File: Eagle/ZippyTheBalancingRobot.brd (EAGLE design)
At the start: 81.3 x 81.3 mm, 33 parts

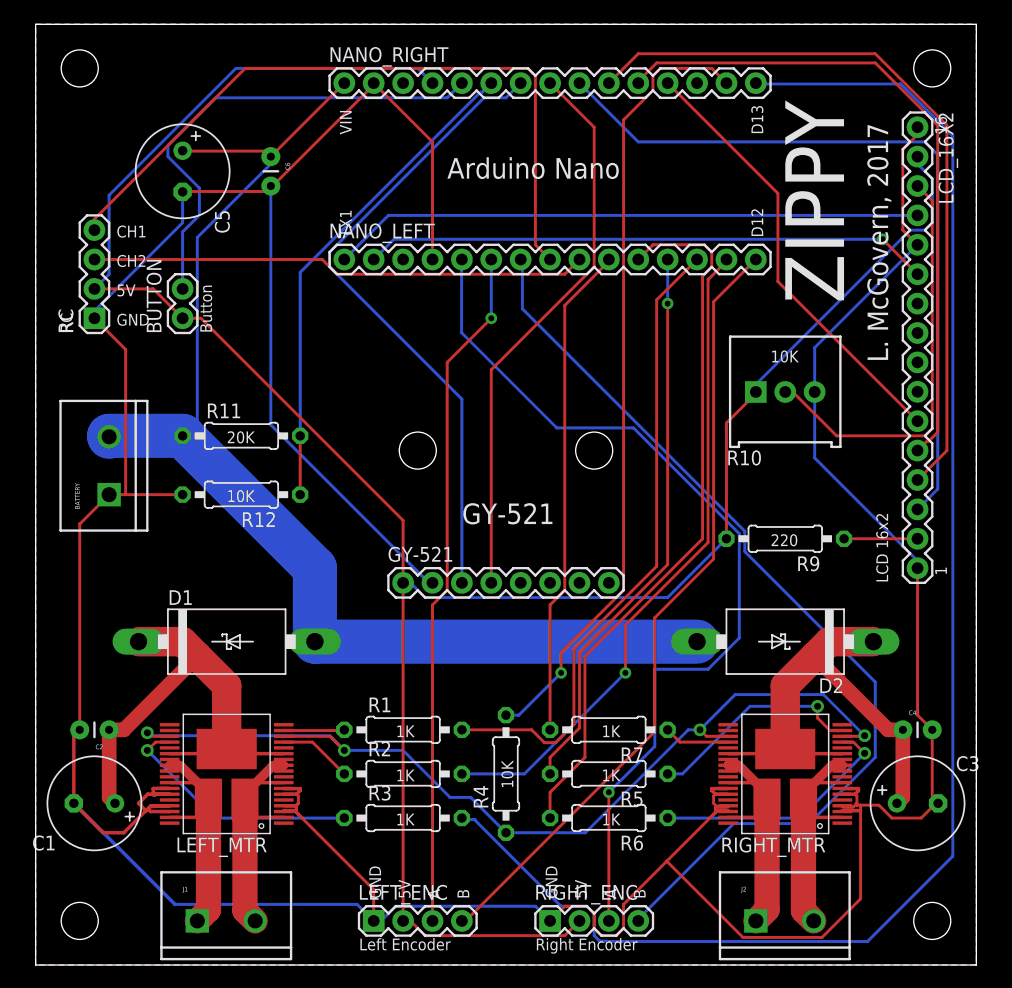
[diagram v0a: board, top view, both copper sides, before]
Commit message: Update code for PCB, and fix PCB errors.
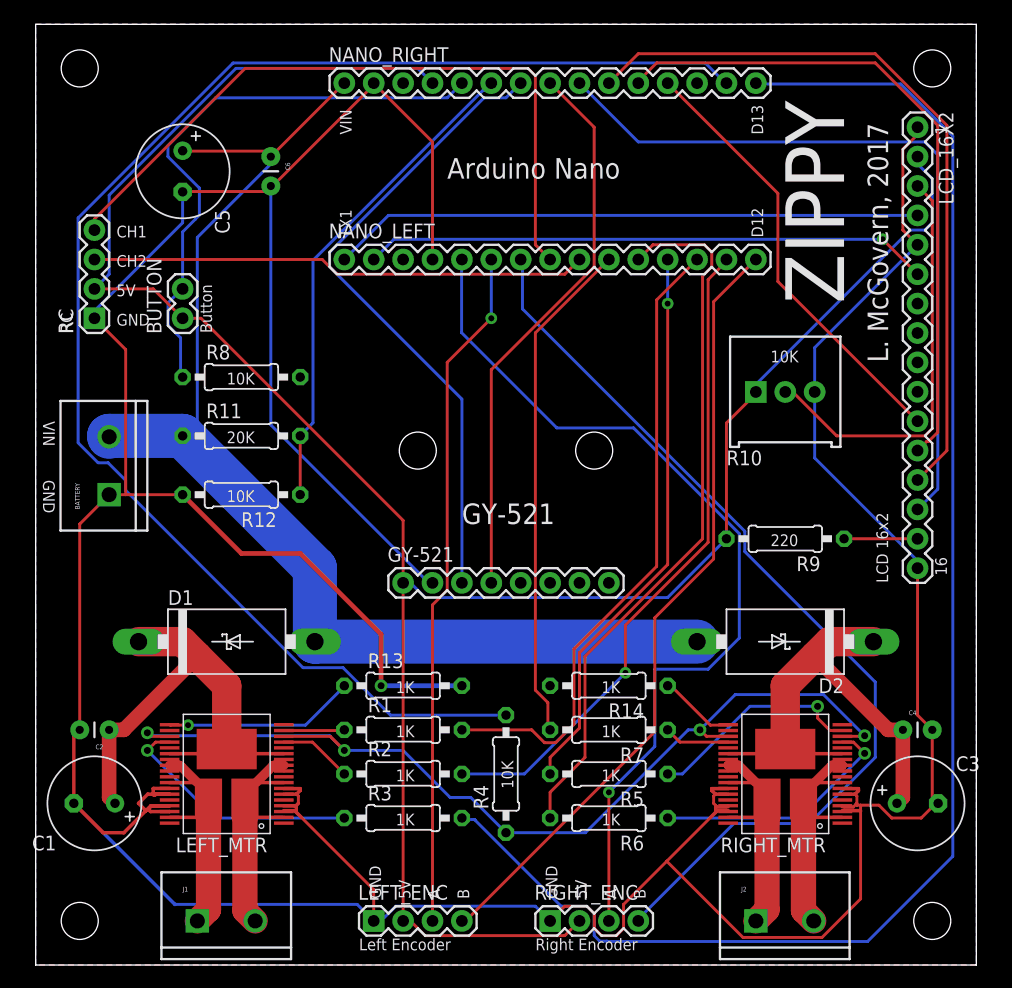
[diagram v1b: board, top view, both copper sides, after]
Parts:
- added R13, R14: 1K, resistor:0207/10
- added R8: 10K, resistor:0207/10
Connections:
- new net N$1: LEFT_MTR.19, R13.1
- new net N$3: R14.1, RIGHT_MTR.19
- net A7: now also R8.1
- net GND: now also R13.2, R14.2, R8.2
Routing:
- net 3.3V: track 68.3 -> 128.9 mm, vias 1 -> 0
- net GND: track 373.4 -> 406.9 mm, vias 0 -> 1
- net N$1: track 0.00 -> 16.5 mm, vias 0 -> 1
- net A7: track 41.7 -> 50.4 mm
- net N$3: track 0.00 -> 6.74 mm
- net D7: track 42.7 -> 43.8 mm
